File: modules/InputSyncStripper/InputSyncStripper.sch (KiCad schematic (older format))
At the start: 14 parts

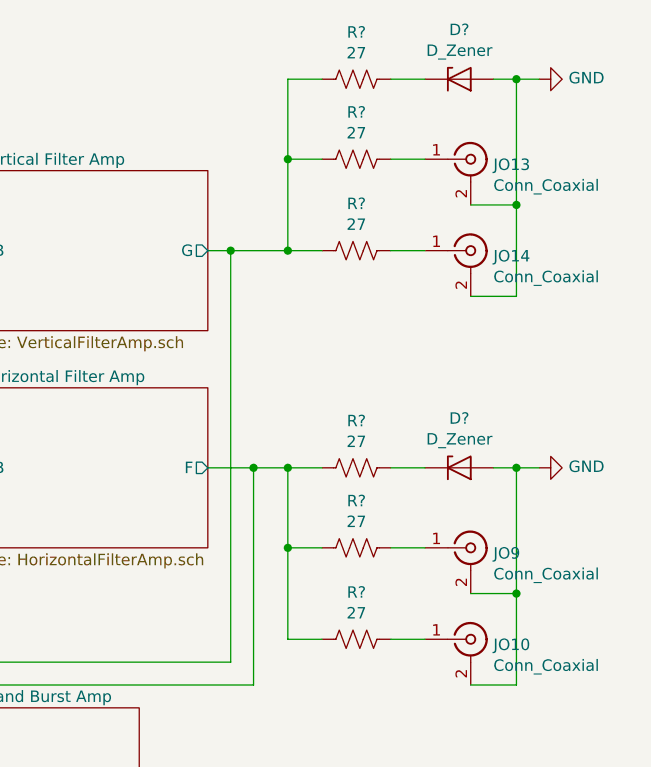
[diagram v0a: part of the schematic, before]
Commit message: fix some ERC issues; assign symbols
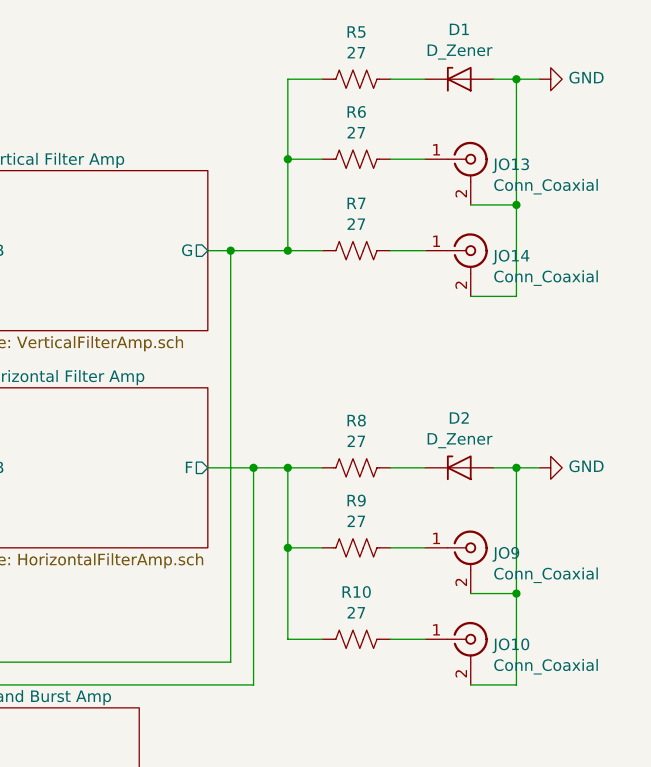
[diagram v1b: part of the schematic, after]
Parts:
- gave numbers to parts that had none: 8
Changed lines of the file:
@@
 EESchema Schematic File Version 4
-LIBS:SIP-cache
+LIBS:InputSyncStripper-cache
 EELAYER 26 0
 EELAYER END
@@
 $EndComp
 $Comp
-L power:GND #PWR?
+L power:GND #PWR02
 U 1 1 5BC7EDA5
 P 1600 1900
-F 0 "#PWR?" H 1600 1650 50  0001 C CNN
+F 0 "#PWR02" H 1600 1650 50  0001 C CNN
 F 1 "GND" H 1605 1727 50  0000 C CNN
 F 2 "" H 1600 1900 50  0001 C CNN
@@
 $EndComp
 $Comp
-L power:GND #PWR?
+L power:GND #PWR01
 U 1 1 5BC7EEDA
 P 1000 1700
-F 0 "#PWR?" H 1000 1450 50  0001 C CNN
+F 0 "#PWR01" H 1000 1450 50  0001 C CNN
 F 1 "GND" H 1005 1527 50  0000 C CNN
 F 2 "" H 1000 1700 50  0001 C CNN
@@
 	3800 2550 3800 1600
 $Comp
-L Device:R_US R?
+L Device:R_US R5
 U 1 1 5BCB0BA6
 P 5900 850
-F 0 "R?" V 5695 850 50  0000 C CNN
+F 0 "R5" V 5695 850 50  0000 C CNN
 F 1 "27" V 5786 850 50  0000 C CNN
 F 2 "" V 5940 840 50  0001 C CNN
@@
 $EndComp
 $Comp
-L Device:R_US R?
+L Device:R_US R6
 U 1 1 5BCB0C2D
 P 5900 1200
-F 0 "R?" V 5695 1200 50  0000 C CNN
+F 0 "R6" V 5695 1200 50  0000 C CNN
 F 1 "27" V 5786 1200 50  0000 C CNN
 F 2 "" V 5940 1190 50  0001 C CNN
@@
 $EndComp
 $Comp
-L Device:R_US R?
+L Device:R_US R7
 U 1 1 5BCB0CDE
 P 5900 1600
-F 0 "R?" V 5695 1600 50  0000 C CNN
+F 0 "R7" V 5695 1600 50  0000 C CNN
 F 1 "27" V 5786 1600 50  0000 C CNN
 F 2 "" V 5940 1590 50  0001 C CNN
@@
 $EndComp
 $Comp
-L Device:D_Zener D?
+L Device:D_Zener D1
 U 1 1 5BCB0E05
 P 6350 850
-F 0 "D?" H 6350 1066 50  0000 C CNN
+F 0 "D1" H 6350 1066 50  0000 C CNN
 F 1 "D_Zener" H 6350 975 50  0000 C CNN
 F 2 "" H 6350 850 50  0001 C CNN
@@
 $EndComp
 $Comp
-L power:GND #PWR?
+L power:GND #PWR03
 U 1 1 5BCB1088
 P 6700 850
-F 0 "#PWR?" H 6700 600 50  0001 C CNN
+F 0 "#PWR03" H 6700 600 50  0001 C CNN
 F 1 "GND" V 6705 722 50  0000 R CNN
 F 2 "" H 6700 850 50  0001 C CNN
@@
 	5600 1200 5600 1600
 $Comp
-L Device:R_US R?
+L Device:R_US R8
 U 1 1 5BCB2490
 P 5900 2550
-F 0 "R?" V 5695 2550 50  0000 C CNN
+F 0 "R8" V 5695 2550 50  0000 C CNN
 F 1 "27" V 5786 2550 50  0000 C CNN
 F 2 "" V 5940 2540 50  0001 C CNN
@@
 $EndComp
 $Comp
-L Device:R_US R?
+L Device:R_US R9
 U 1 1 5BCB2496
 P 5900 2900
-F 0 "R?" V 5695 2900 50  0000 C CNN
+F 0 "R9" V 5695 2900 50  0000 C CNN
 F 1 "27" V 5786 2900 50  0000 C CNN
 F 2 "" V 5940 2890 50  0001 C CNN
@@
 $EndComp
 $Comp
-L Device:R_US R?
+L Device:R_US R10
 U 1 1 5BCB249C
 P 5900 3300
-F 0 "R?" V 5695 3300 50  0000 C CNN
+F 0 "R10" V 5695 3300 50  0000 C CNN
 F 1 "27" V 5786 3300 50  0000 C CNN
 F 2 "" V 5940 3290 50  0001 C CNN
@@
 $EndComp
 $Comp
-L Device:D_Zener D?
+L Device:D_Zener D2
 U 1 1 5BCB24A2
 P 6350 2550
-F 0 "D?" H 6350 2766 50  0000 C CNN
+F 0 "D2" H 6350 2766 50  0000 C CNN
 F 1 "D_Zener" H 6350 2675 50  0000 C CNN
 F 2 "" H 6350 2550 50  0001 C CNN
@@
 $EndComp
 $Comp
-L power:GND #PWR?
+L power:GND #PWR04
 U 1 1 5BCB24B4
 P 6700 2550
-F 0 "#PWR?" H 6700 2300 50  0001 C CNN
+F 0 "#PWR04" H 6700 2300 50  0001 C CNN
 F 1 "GND" V 6705 2422 50  0000 R CNN
 F 2 "" H 6700 2550 50  0001 C CNN

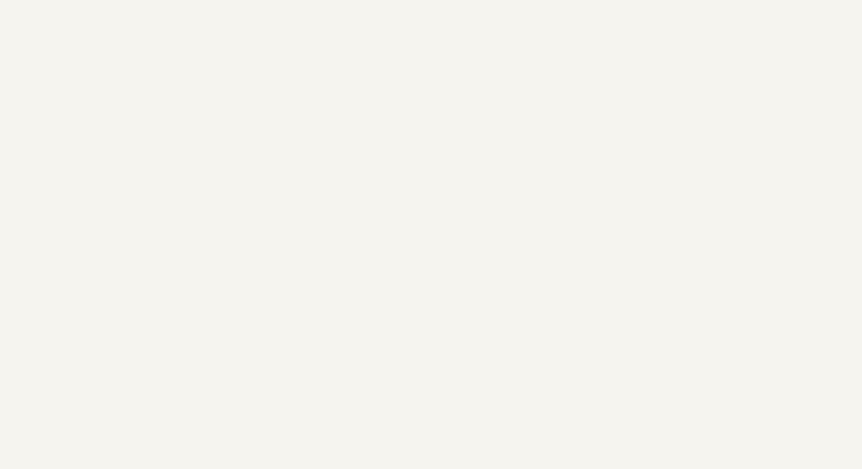
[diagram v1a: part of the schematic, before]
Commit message: added power flags and power connector
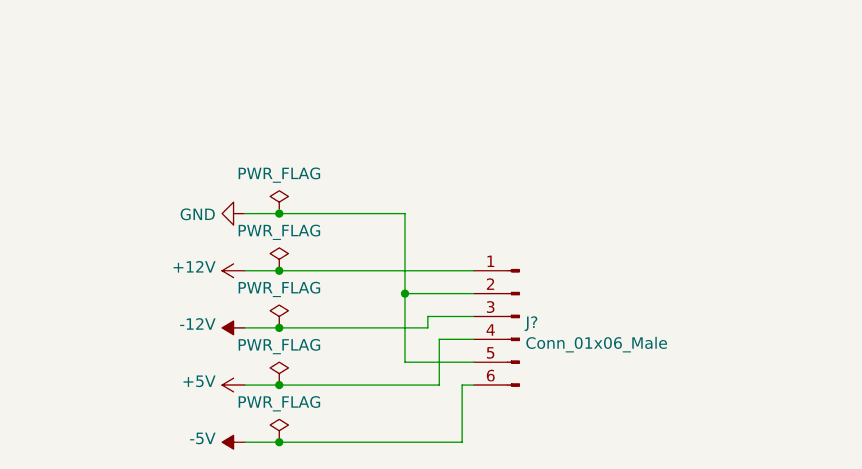
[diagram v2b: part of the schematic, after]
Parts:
- added J?: Conn_01x06_Male, symbol Connector:Conn_01x06_Male
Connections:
- net GND: now also J?.2 (Pin_2), J?.5 (Pin_5)
- new net +12V: J?.1 (Pin_1)
- new net +5V: J?.4 (Pin_4)
- new net -12V: J?.3 (Pin_3)
- new net -5V: J?.6 (Pin_6)
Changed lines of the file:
@@
 Wire Wire Line
 	5350 1600 5600 1600
+$Comp
+L power:GND #PWR0105
+U 1 1 5BCE2417
+P 2400 5700
+F 0 "#PWR0105" H 2400 5450 50  0001 C CNN
+F 1 "GND" V 2405 5572 50  0000 R CNN
+F 2 "" H 2400 5700 50  0001 C CNN
+F 3 "" H 2400 5700 50  0001 C CNN
+	1    2400 5700
+	0    1    1    0
+$EndComp
+$Comp
+L power:+12V #PWR0106
+U 1 1 5BCE24C5
+P 2400 5950
+F 0 "#PWR0106" H 2400 5800 50  0001 C CNN
+F 1 "+12V" V 2415 6078 50  0000 L CNN
+F 2 "" H 2400 5950 50  0001 C CNN
+F 3 "" H 2400 5950 50  0001 C CNN
+	1    2400 5950
+	0    -1   -1   0
+$EndComp
+$Comp
+L power:-12V #PWR0107
+U 1 1 5BCE258F
+P 2400 6200
+F 0 "#PWR0107" H 2400 6300 50  0001 C CNN
+F 1 "-12V" V 2415 6328 50  0000 L CNN
+F 2 "" H 2400 6200 50  0001 C CNN
+F 3 "" H 2400 6200 50  0001 C CNN
+	1    2400 6200
+	0    -1   -1   0
+$EndComp
+$Comp
+L power:+5V #PWR0108
+U 1 1 5BCE2660
+P 2400 6450
+F 0 "#PWR0108" H 2400 6300 50  0001 C CNN
+F 1 "+5V" V 2415 6578 50  0000 L CNN
+F 2 "" H 2400 6450 50  0001 C CNN
+F 3 "" H 2400 6450 50  0001 C CNN
+	1    2400 6450
+	0    -1   -1   0
+$EndComp
+Wire Wire Line
+	2400 5700 2550 5700
+Wire Wire Line
+	2400 5950 2550 5950
+Wire Wire Line
+	2400 6200 2550 6200
+Wire Wire Line
+	2400 6450 2550 6450
+$Comp
+L power:PWR_FLAG #FLG0101
+U 1 1 5BCE641F
+P 2550 6450
+F 0 "#FLG0101" H 2550 6525 50  0001 C CNN
+F 1 "PWR_FLAG" H 2550 6624 50  0000 C CNN
+F 2 "" H 2550 6450 50  0001 C CNN
+F 3 "~" H 2550 6450 50  0001 C CNN
+	1    2550 6450
+	1    0    0    -1
+$EndComp
+Connection ~ 2550 6450
+$Comp
+L power:PWR_FLAG #FLG0102
+U 1 1 5BCE646D
+P 2550 6200
+F 0 "#FLG0102" H 2550 6275 50  0001 C CNN
+F 1 "PWR_FLAG" H 2550 6374 50  0000 C CNN
+F 2 "" H 2550 6200 50  0001 C CNN
+F 3 "~" H 2550 6200 50  0001 C CNN
+	1    2550 6200
+	1    0    0    -1
+$EndComp
+Connection ~ 2550 6200
+$Comp
+L power:PWR_FLAG #FLG0103
+U 1 1 5BCE64BB
+P 2550 5950
+F 0 "#FLG0103" H 2550 6025 50  0001 C CNN
+F 1 "PWR_FLAG" H 2550 6124 50  0000 C CNN
+F 2 "" H 2550 5950 50  0001 C CNN
+F 3 "~" H 2550 5950 50  0001 C CNN
+	1    2550 5950
+	1    0    0    -1
+$EndComp
+Connection ~ 2550 5950
+$Comp
+L power:PWR_FLAG #FLG0104
+U 1 1 5BCE6509
+P 2550 5700
+F 0 "#FLG0104" H 2550 5775 50  0001 C CNN
+F 1 "PWR_FLAG" H 2550 5874 50  0000 C CNN
+F 2 "" H 2550 5700 50  0001 C CNN
+F 3 "~" H 2550 5700 50  0001 C CNN
+	1    2550 5700
+	1    0    0    -1
+$EndComp
+Connection ~ 2550 5700
+$Comp
+L power:-5V #PWR?
+U 1 1 5BCE65B9
+P 2400 6700
+F 0 "#PWR?" H 2400 6800 50  0001 C CNN
+F 1 "-5V" V 2415 6828 50  0000 L CNN
+F 2 "" H 2400 6700 50  0001 C CNN
+F 3 "" H 2400 6700 50  0001 C CNN
+	1    2400 6700
+	0    -1   -1   0
+$EndComp
+Wire Wire Line
+	2400 6700 2550 6700
+$Comp
+L power:PWR_FLAG #FLG?
+U 1 1 5BCE7B53
+P 2550 6700
+F 0 "#FLG?" H 2550 6775 50  0001 C CNN
+F 1 "PWR_FLAG" H 2550 6874 50  0000 C CNN
+F 2 "" H 2550 6700 50  0001 C CNN
+F 3 "~" H 2550 6700 50  0001 C CNN
+	1    2550 6700
+	1    0    0    -1
+$EndComp
+Connection ~ 2550 6700
+$Comp
+L Connector:Conn_01x06_Male J?
+U 1 1 5BCE7BE7
+P 3600 6150
+F 0 "J?" H 3573 6123 50  0000 R CNN
+F 1 "Conn_01x06_Male" H 3573 6032 50  0000 R CNN
+F 2 "" H 3600 6150 50  0001 C CNN
+F 3 "~" H 3600 6150 50  0001 C CNN
+	1    3600 6150
+	-1   0    0    -1
+$EndComp
+Wire Wire Line
+	2550 5950 3400 5950
+Wire Wire Line
+	3100 5700 3100 6050
+Wire Wire Line
+	3100 6050 3400 6050
+Wire Wire Line
+	2550 5700 3100 5700
+Wire Wire Line
+	3100 6050 3100 6350
+Wire Wire Line
+	3100 6350 3400 6350
+Connection ~ 3100 6050
+Wire Wire Line
+	3200 6200 3200 6150
+Wire Wire Line
+	3200 6150 3400 6150
+Wire Wire Line
+	2550 6200 3200 6200
+Wire Wire Line
+	3250 6450 3250 6250
+Wire Wire Line
+	3250 6250 3400 6250
+Wire Wire Line
+	2550 6450 3250 6450
+Wire Wire Line
+	3350 6700 3350 6450
+Wire Wire Line
+	3350 6450 3400 6450
+Wire Wire Line
+	2550 6700 3350 6700
 $EndSCHEMATC

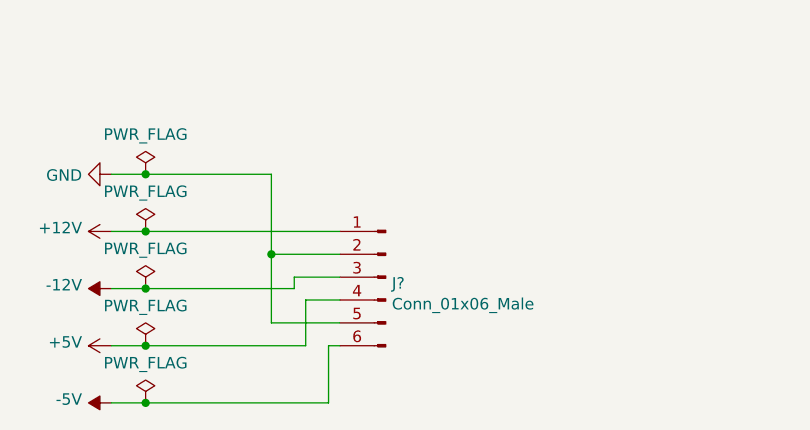
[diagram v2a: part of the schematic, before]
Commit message: added power pins for opamps and tied inputs of unused amp
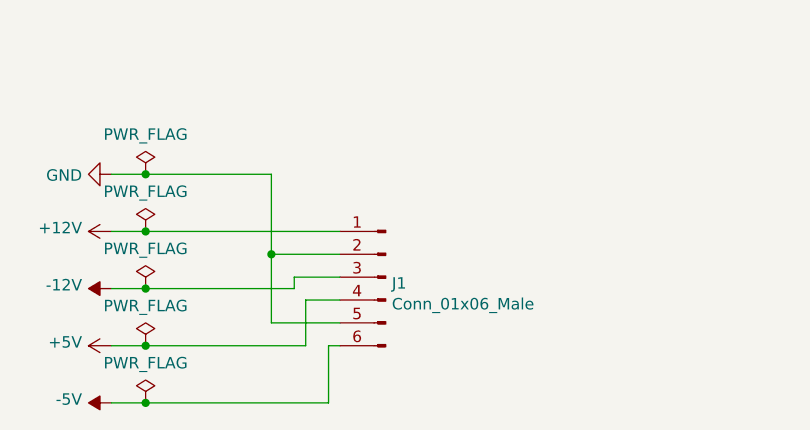
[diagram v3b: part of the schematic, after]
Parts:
- gave numbers to parts that had none: 1
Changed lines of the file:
@@
 Connection ~ 2550 5700
 $Comp
-L power:-5V #PWR?
+L power:-5V #PWR0109
 U 1 1 5BCE65B9
 P 2400 6700
-F 0 "#PWR?" H 2400 6800 50  0001 C CNN
+F 0 "#PWR0109" H 2400 6800 50  0001 C CNN
 F 1 "-5V" V 2415 6828 50  0000 L CNN
 F 2 "" H 2400 6700 50  0001 C CNN
@@
 	2400 6700 2550 6700
 $Comp
-L power:PWR_FLAG #FLG?
+L power:PWR_FLAG #FLG0105
 U 1 1 5BCE7B53
 P 2550 6700
-F 0 "#FLG?" H 2550 6775 50  0001 C CNN
+F 0 "#FLG0105" H 2550 6775 50  0001 C CNN
 F 1 "PWR_FLAG" H 2550 6874 50  0000 C CNN
 F 2 "" H 2550 6700 50  0001 C CNN
@@
 Connection ~ 2550 6700
 $Comp
-L Connector:Conn_01x06_Male J?
+L Connector:Conn_01x06_Male J1
 U 1 1 5BCE7BE7
 P 3600 6150
-F 0 "J?" H 3573 6123 50  0000 R CNN
+F 0 "J1" H 3573 6123 50  0000 R CNN
 F 1 "Conn_01x06_Male" H 3573 6032 50  0000 R CNN
 F 2 "" H 3600 6150 50  0001 C CNN
